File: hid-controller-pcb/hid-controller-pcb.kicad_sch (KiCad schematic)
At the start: 65 parts, among them IC1 RT9080-33GJ5, J1 10118194-0011LF, J2 Jumper, J3 STLink, U1 STM32F103C8Tx, U3 COM-09032, U4 COM-09032, Y1 8MHz, Y2 32.768KHz

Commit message: final version of controller v1.0
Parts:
- added C15, C16, C17, C18: 0.1uF, Capacitor_SMD:C_0805_2012Metric_Pad1.18x1.45mm_HandSolder, symbol Device:C_Small
- added R26: 10kR, Resistor_SMD:R_0805_2012Metric_Pad1.20x1.40mm_HandSolder, symbol Device:R_Small
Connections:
- net AN_A1: now also C16.1
- net AN_A2: now also C17.1
- net AN_B1: now also C15.1
- net AN_B2: now also C18.1
- net BOOT0: now also R26.2; no longer J2.2 (Pin_2)
- net BTN_RB: now also U1.26 (PB13); no longer U1.28 (PB15)
- net BTN_RT: now also U1.28 (PB15); no longer U1.26 (PB13)
- net GND: now also C15.2, C16.2, C17.2, C18.2
- new net: J2.2 (Pin_2), R26.1

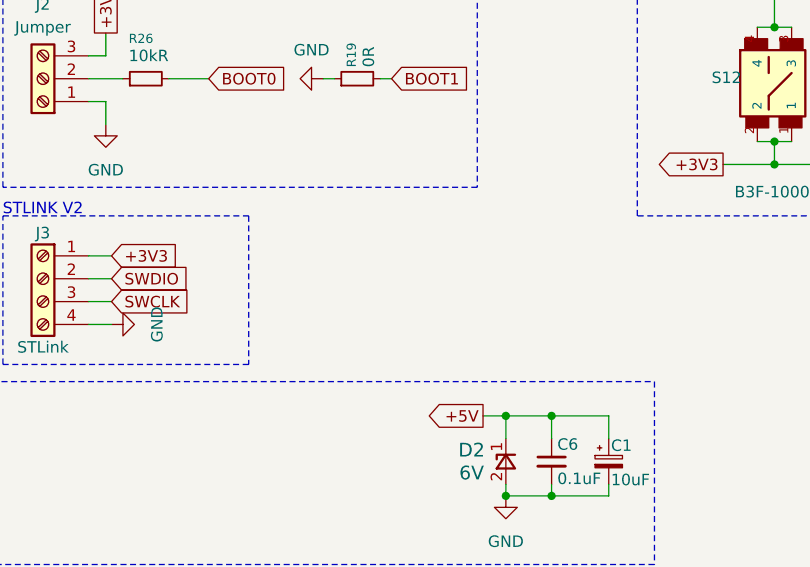
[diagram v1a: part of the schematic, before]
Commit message: makefile linux gcc path fix
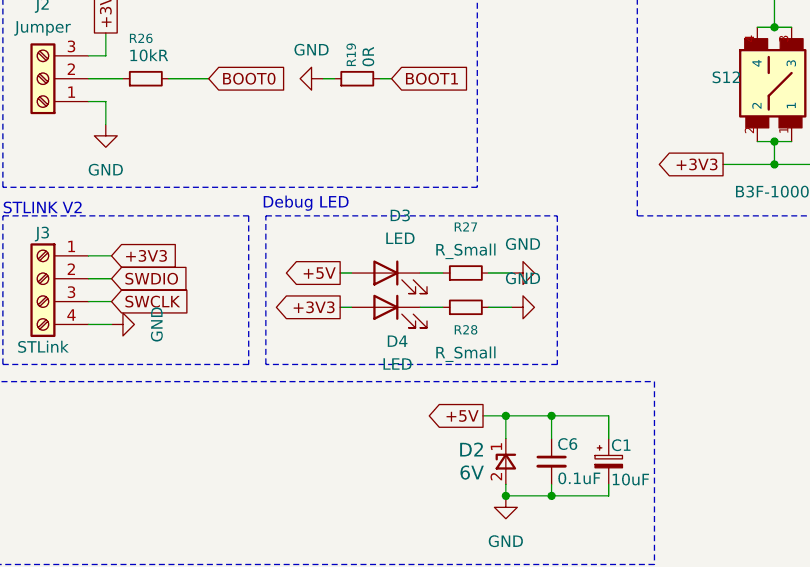
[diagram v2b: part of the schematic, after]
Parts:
- added D3, D4: LED, LED_SMD:LED_0805_2012Metric, symbol Device:LED
- added R27, R28: R_Small, Resistor_SMD:R_0805_2012Metric_Pad1.20x1.40mm_HandSolder, symbol Device:R_Small
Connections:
- net +3V3: now also D4.2 (A)
- net +5V: now also D3.2 (A)
- net GND: now also R27.2, R28.2
- new net: D4.1 (K), R28.1
- new net: D3.1 (K), R27.1
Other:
- note added: "Debug LED"
